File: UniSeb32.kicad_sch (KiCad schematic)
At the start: 57 parts, among them J1 IO, J2 ARJM11C7-114-BA-EW2, J3 Conn_02x05_Odd_Even, J6 SDS011, J7 Conn_01x02_Female, J8 Conn_01x02_Female, U1 mini_esp32, U2 LAN8720A, U3 AMS1117-3.3, U4 AMS5919, U5 module_bme280, U6 RT9400, U7 MCP23008-xSS, U8 HLK-PM01, X1 233-508, X2 233-503, X3 233-504, Y1 Crystal_GND23

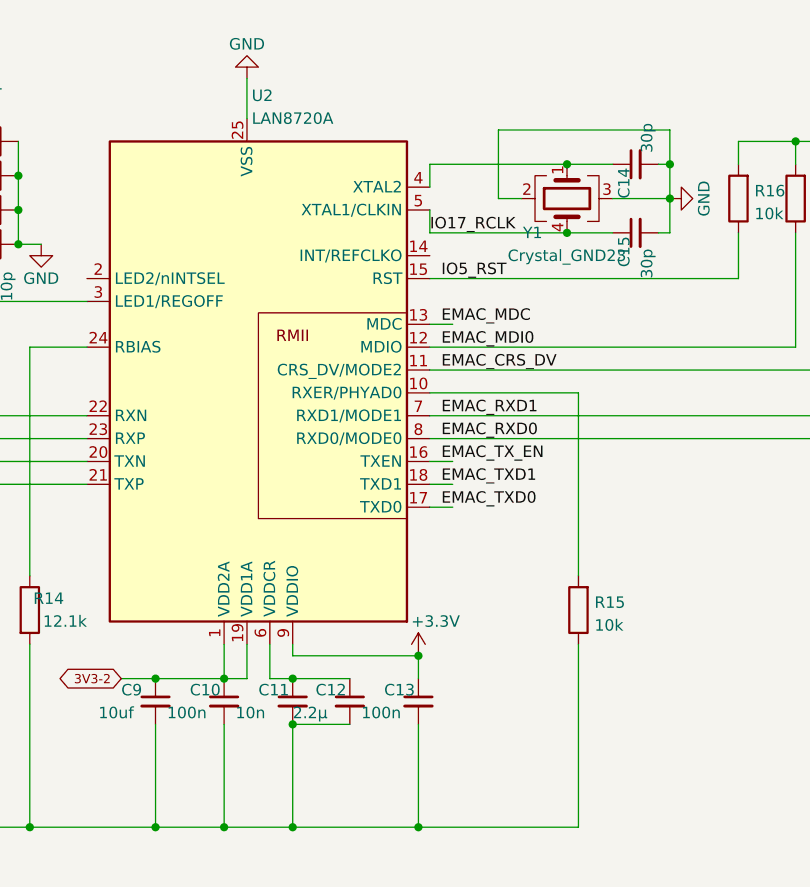
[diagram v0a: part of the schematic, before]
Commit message: Fixes wrong pin numbering at Y1
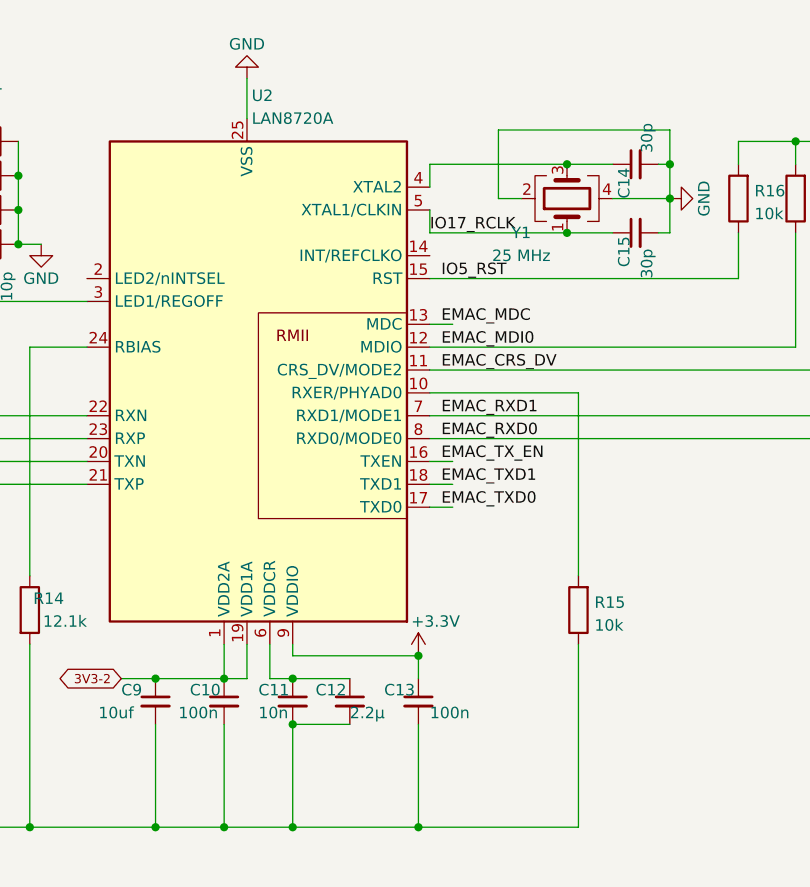
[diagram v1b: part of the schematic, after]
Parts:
- removed Y1: Crystal_GND23, Crystal:Crystal_SMD_3225-4Pin_3.2x2.5mm, symbol Device:Crystal_GND23
- added Y1: 25 MHz, Crystal:Crystal_SMD_3225-4Pin_3.2x2.5mm, symbol Device:Crystal_GND24
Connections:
- net GND: now also Y1.2, Y1.4
- net IO17_RCLK: now also Y1.1
- net at C14.1, U2.4 (XTAL2): now also Y1.3
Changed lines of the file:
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@@
   (junction (at 152.4 325.12) (diameter 0) (color 0 0 0 0)
   )
+  (junction (at 212.09 259.08) (diameter 0) (color 0 0 0 0)
+  )
   (junction (at 135.89 236.22) (diameter 0) (color 0 0 0 0)
   )
@@
   (junction (at 180.34 97.155) (diameter 0) (color 0 0 0 0)
   )
-  (junction (at 212.09 251.46) (diameter 0) (color 0 0 0 0)
-  )
   (junction (at 255.27 91.44) (diameter 0) (color 0 0 0 0)
   )
@@
   (junction (at 85.725 138.43) (diameter 0) (color 0 0 0 0)
   )
-  (junction (at 212.09 259.08) (diameter 0) (color 0 0 0 0)
-  )
   (junction (at 173.99 325.12) (diameter 0) (color 0 0 0 0)
   )
@@
   (junction (at 162.56 185.42) (diameter 0) (color 0 0 0 0)
   )
+  (junction (at 212.09 251.46) (diameter 0) (color 0 0 0 0)
+  )
   (junction (at 162.56 182.88) (diameter 0) (color 0 0 0 0)
   )
@@
     (stroke (width 0) (type default) (color 0 0 0 0))
   )
+  (wire (pts (xy 212.09 251.46) (xy 217.17 251.46))
+    (stroke (width 0) (type default) (color 0 0 0 0))
+  )
   (wire (pts (xy 127 289.56) (xy 129.54 289.56))
     (stroke (width 0) (type default) (color 0 0 0 0))
@@
     (stroke (width 0) (type default) (color 0 0 0 0))
   )
-  (wire (pts (xy 212.09 259.08) (xy 217.17 259.08))
+  (wire (pts (xy 196.85 259.08) (xy 212.09 259.08))
     (stroke (width 0) (type default) (color 0 0 0 0))
   )
@@
     (stroke (width 0) (type default) (color 0 0 0 0))
   )
-  (wire (pts (xy 196.85 251.46) (xy 212.09 251.46))
-    (stroke (width 0) (type default) (color 0 0 0 0))
-  )
   (wire (pts (xy 237.49 248.92) (xy 237.49 251.46))
     (stroke (width 0) (type default) (color 0 0 0 0))
@@
     (stroke (width 0) (type default) (color 0 0 0 0))
   )
-  (wire (pts (xy 212.09 251.46) (xy 217.17 251.46))
+  (wire (pts (xy 196.85 251.46) (xy 212.09 251.46))
     (stroke (width 0) (type default) (color 0 0 0 0))
   )
@@
     (stroke (width 0) (type default) (color 0 0 0 0))
   )
-  (wire (pts (xy 129.54 246.38) (xy 129.54 255.27))
+  (wire (pts (xy 212.09 259.08) (xy 217.17 259.08))
     (stroke (width 0) (type default) (color 0 0 0 0))
   )
-  (wire (pts (xy 196.85 259.08) (xy 212.09 259.08))
+  (wire (pts (xy 129.54 246.38) (xy 129.54 255.27))
     (stroke (width 0) (type default) (color 0 0 0 0))
   )
@@
     (pin "8")
   )
+  (symbol (lib_id "Device:Crystal_GND24") (at 212.09 255.27 90) (unit 1)
+    (in_bom yes) (on_board yes)
+    (property "Reference" "Y1" (id 0) (at 207.01 259.08 90))
+    (property "Value" "25 MHz" (id 1) (at 207.01 261.62 90))
+    (property "Footprint" "Crystal:Crystal_SMD_3225-4Pin_3.2x2.5mm" (id 2) (at 212.09 255.27 0)
+      (effects (font (size 1.27 1.27)) hide)
+    )
+    (property "Datasheet" "~" (id 3) (at 212.09 255.27 0)
+      (effects (font (size 1.27 1.27)) hide)
+    )
+    (property "LCSC" "C9006" (id 4) (at 212.09 255.27 90)
+      (effects (font (size 1.27 1.27)) hide)
+    )
+    (property "JLC" "3225" (id 5) (at 212.09 255.27 90)
+      (effects (font (size 1.27 1.27)) hide)
+    )
+    (pin "1")
+    (pin "2")
+    (pin "3")
+    (pin "4")
+  )
   (symbol (lib_id "Device:L") (at 101.6 91.44 90) (unit 1)
     (in_bom yes) (on_board yes) (fields_autoplaced)
@@
       (effects (font (size 1.27 1.27)) (justify left))
     )
-    (property "Value" "100n" (id 1) (at 167.64 312.42 0)
+    (property "Value" "100n" (id 1) (at 168.91 312.42 0)
       (effects (font (size 1.27 1.27)) (justify left))
     )
@@
       (effects (font (size 1.27 1.27)) (justify left))
     )
-    (property "Value" "2.2µ" (id 1) (at 181.61 312.42 0)
+    (property "Value" "2.2µ" (id 1) (at 187.96 312.42 0)
       (effects (font (size 1.27 1.27)) (justify left))
     )
@@
     (pin "2")
   )
-  (symbol (lib_id "Device:Crystal_GND23") (at 212.09 255.27 90) (mirror x) (unit 1)
-    (in_bom yes) (on_board yes)
-    (property "Reference" "Y1" (id 0) (at 208.28 259.08 90))
-    (property "Value" "Crystal_GND23" (id 1) (at 212.09 261.62 90))
-    (property "Footprint" "Crystal:Crystal_SMD_3225-4Pin_3.2x2.5mm" (id 2) (at 212.09 255.27 0)
-      (effects (font (size 1.27 1.27)) hide)
-    )
-    (property "Datasheet" "~" (id 3) (at 212.09 255.27 0)
-      (effects (font (size 1.27 1.27)) hide)
-    )
-    (property "LCSC" "C9006" (id 4) (at 212.09 255.27 90)
-      (effects (font (size 1.27 1.27)) hide)
-    )
-    (property "JLC" "3225" (id 5) (at 212.09 255.27 90)
-      (effects (font (size 1.27 1.27)) hide)
-    )
-    (pin "1")
-    (pin "2")
-    (pin "3")
-    (pin "4")
-  )
   (symbol (lib_id "con-wago:233-508") (at 216.535 86.995 0) (unit 1)
     (in_bom yes) (on_board yes)
@@
       (effects (font (size 1.27 1.27)) (justify left))
     )
-    (property "Value" "100n" (id 1) (at 189.23 312.42 0)
+    (property "Value" "100n" (id 1) (at 196.85 312.42 0)
       (effects (font (size 1.27 1.27)) (justify left))
     )
@@
       (effects (font (size 1.27 1.27)) (justify left))
     )
-    (property "Value" "10n" (id 1) (at 175.26 312.42 0)
+    (property "Value" "10n" (id 1) (at 177.8 312.42 0)
       (effects (font (size 1.27 1.27)) (justify left))
     )
@@
       (reference "X3") (unit 1) (value "233-504") (footprint "con-wago:con-wago-233-504")
     )
-    (path "/648d82f9-455d-4bac-9c2e-2830e45766f8"
-      (reference "Y1") (unit 1) (value "Crystal_GND23") (footprint "Crystal:Crystal_SMD_3225-4Pin_3.2x2.5mm")
+    (path "/0e12f361-782d-4c3b-9962-2932116690ca"
+      (reference "Y1") (unit 1) (value "25 MHz") (footprint "Crystal:Crystal_SMD_3225-4Pin_3.2x2.5mm")
     )
   )

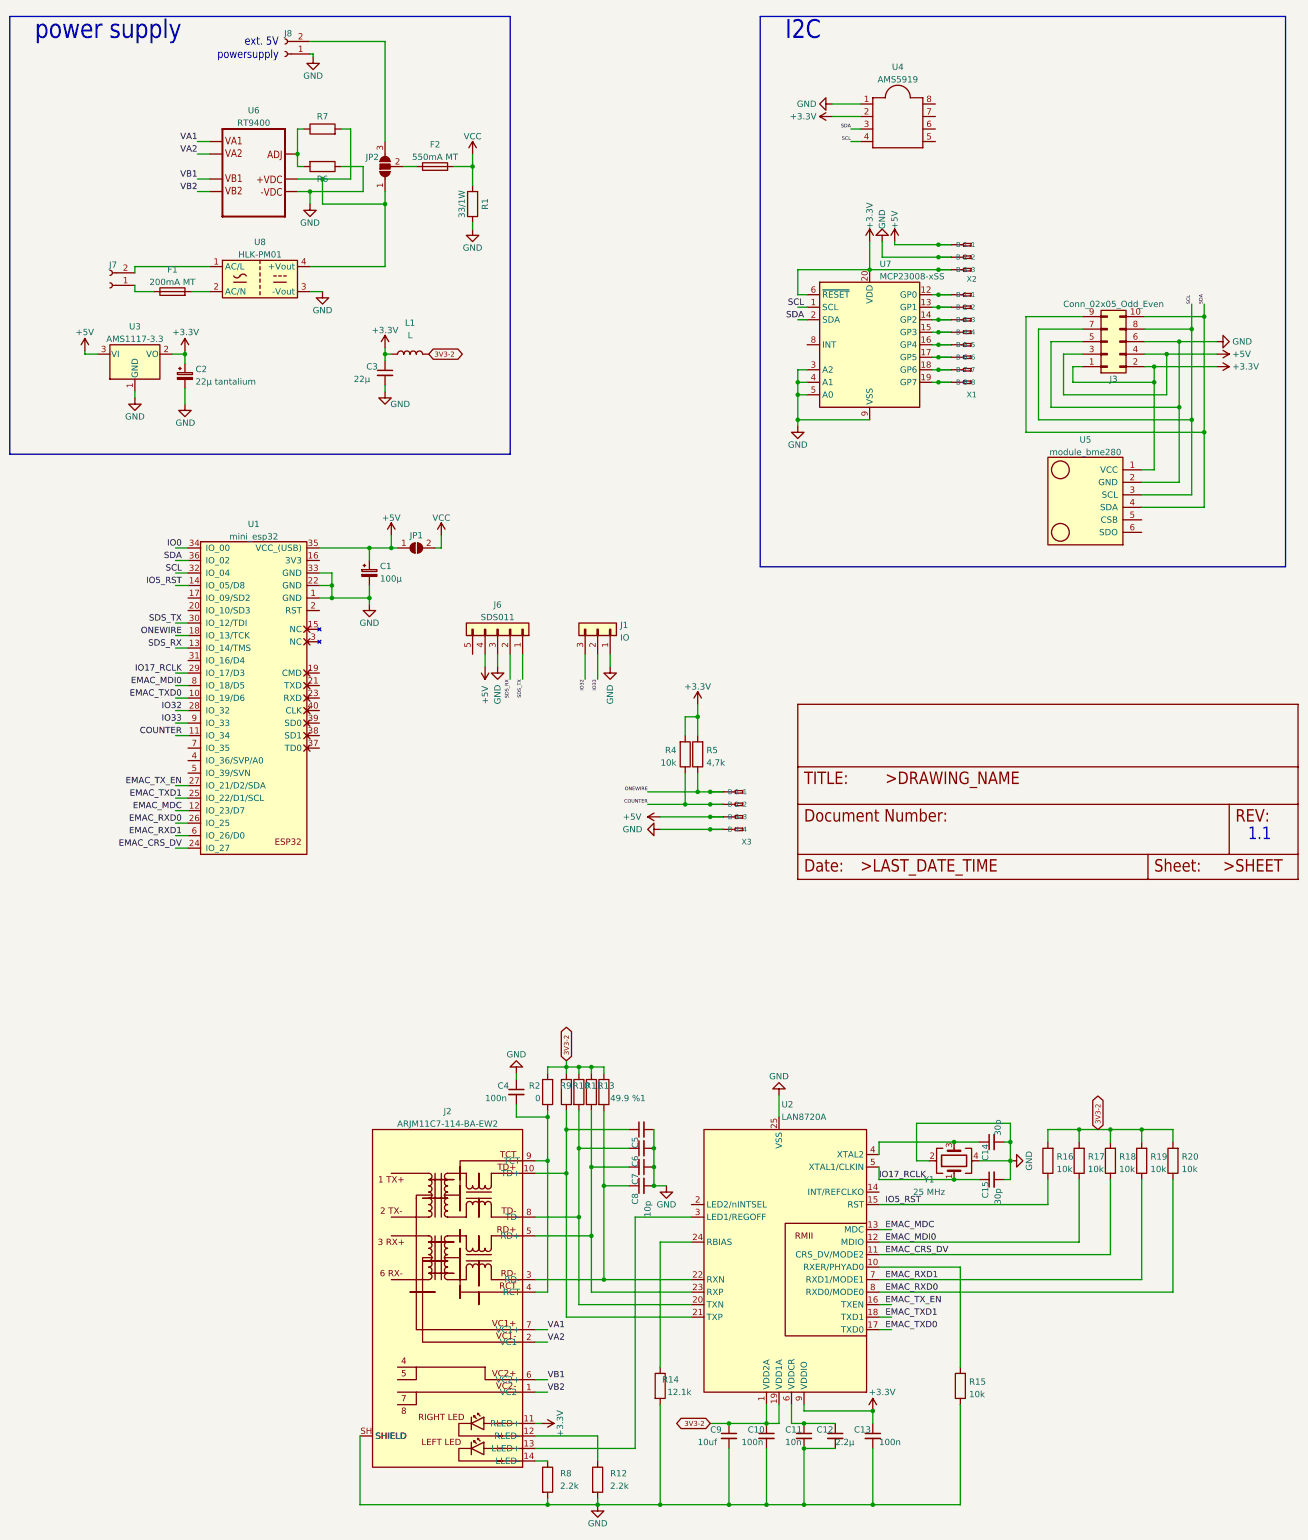
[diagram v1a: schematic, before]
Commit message: corrected mapping of pins added SD slot removed crystal y1 and capacitors in bom and cpl file
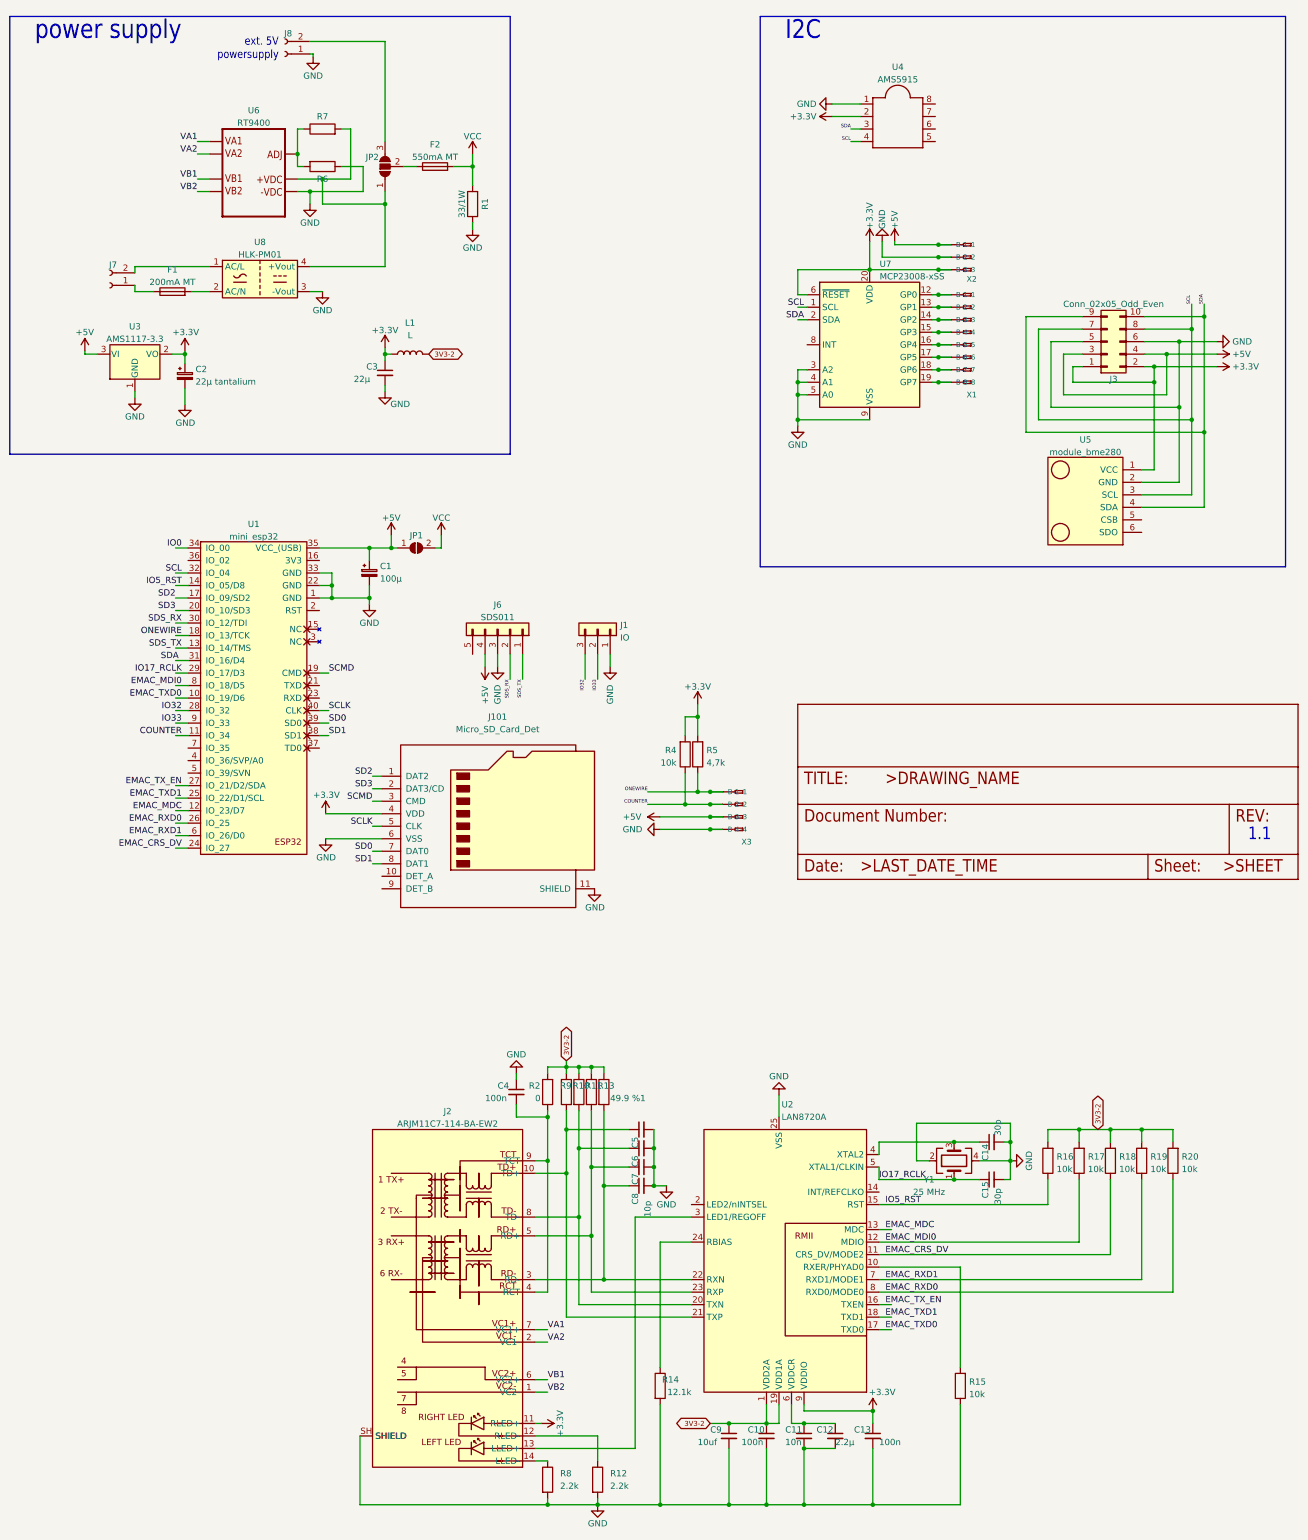
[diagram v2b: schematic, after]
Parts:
- added J101: Micro_SD_Card_Det, Connector_Card:microSD_HC_Hirose_DM3D-SF, symbol Connector:Micro_SD_Card_Det
- C14, C15: JLC 0603 -> (none); LCSC C1658 -> (none)
- U4: value AMS5919 -> AMS5915
- Y1: JLC 3225 -> (none); LCSC C9006 -> (none)
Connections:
- net +3.3V: now also J101.4 (VDD)
- net GND: now also J101.11 (SHIELD), J101.6 (VSS)
- net SDA: now also U1.31 (IO_16/D4); no longer U1.36 (IO_02)
- net SDS_RX: now also U1.30 (IO_12/TDI); no longer U1.13 (IO_14/TMS)
- net SDS_TX: now also U1.13 (IO_14/TMS); no longer U1.30 (IO_12/TDI)
- net SD2: now reaches U1.17 (IO_09/SD2)
- net SD2: now also J101.1 (DAT2)
- net SCMD: now reaches U1.19 (CMD)
- net SCMD: now also J101.3 (CMD)
- net SD3: now reaches U1.20 (IO_10/SD3)
- net SD3: now also J101.2 (DAT3/CD)
- net SD1: now reaches U1.38 (SD1)
- net SD1: now also J101.8 (DAT1)
- net SD0: now reaches U1.39 (SD0)
- net SD0: now also J101.7 (DAT0)
- net SCLK: now reaches U1.40 (CLK)
- net SCLK: now also J101.5 (CLK)

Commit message: .
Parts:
- removed R2: 0, Resistor_SMD:R_0603_1608Metric, symbol Device:R
- added JP?: SolderJumper_2_Open, Jumper:SolderJumper-2_P1.3mm_Open_Pad1.0x1.5mm, symbol Jumper:SolderJumper_2_Open
- C5, C6, C7, C8: JLC 0603 -> (none); LCSC C1634 -> (none)
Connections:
- net +3.3V: now also JP?.1 (A), JP?.2 (B)
- net 3V3-2: now also C4.2, J2.4 (RCT), J2.9 (TCT)
- net IO33: now also J1.3 (Pin_3); no longer J1.2 (Pin_2)
- net IO35: now reaches U1.7 (IO_35)
- net IO35: now also J1.2 (Pin_2)
- net IO32: no longer names the net of U1.28 (IO_32)
- net IO32: no longer J1.3 (Pin_3)
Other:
- moved on the sheet: C4

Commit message: .
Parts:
- removed C15: 30p, Capacitor_SMD:C_0603_1608Metric, symbol Device:C_Small
- removed Y1: 25 MHz, Crystal:Crystal_SMD_3225-4Pin_3.2x2.5mm, symbol Device:Crystal_GND24
- C14: value 30p -> 1n; JLC (none) -> 1206; LCSC (none) -> C9196
- C9: value 10uf -> 10u
- gave numbers to parts that had none: 1
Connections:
- net +3.3V: no longer J2.11 (RLED+)
- net 3V3-2: now also J2.11 (RLED+)
- net GND: no longer J2.SH (SHIELD)
- net at U2.4 (XTAL2): no longer C14.1
- new net: C14.1, J2.SH (SHIELD)
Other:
- moved on the sheet: C4
